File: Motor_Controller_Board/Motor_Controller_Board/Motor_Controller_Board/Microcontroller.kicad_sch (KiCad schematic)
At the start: 26 parts, among them J301 Conn_01x04, J302 USB_B_Micro, J303 Conn_01x02, J304 Conn_01x02, J305 Conn_01x02, SW301 SW_Push, SW302 SW_Push, U301 AMS1117, U302 ESP32-C6-MINI-1

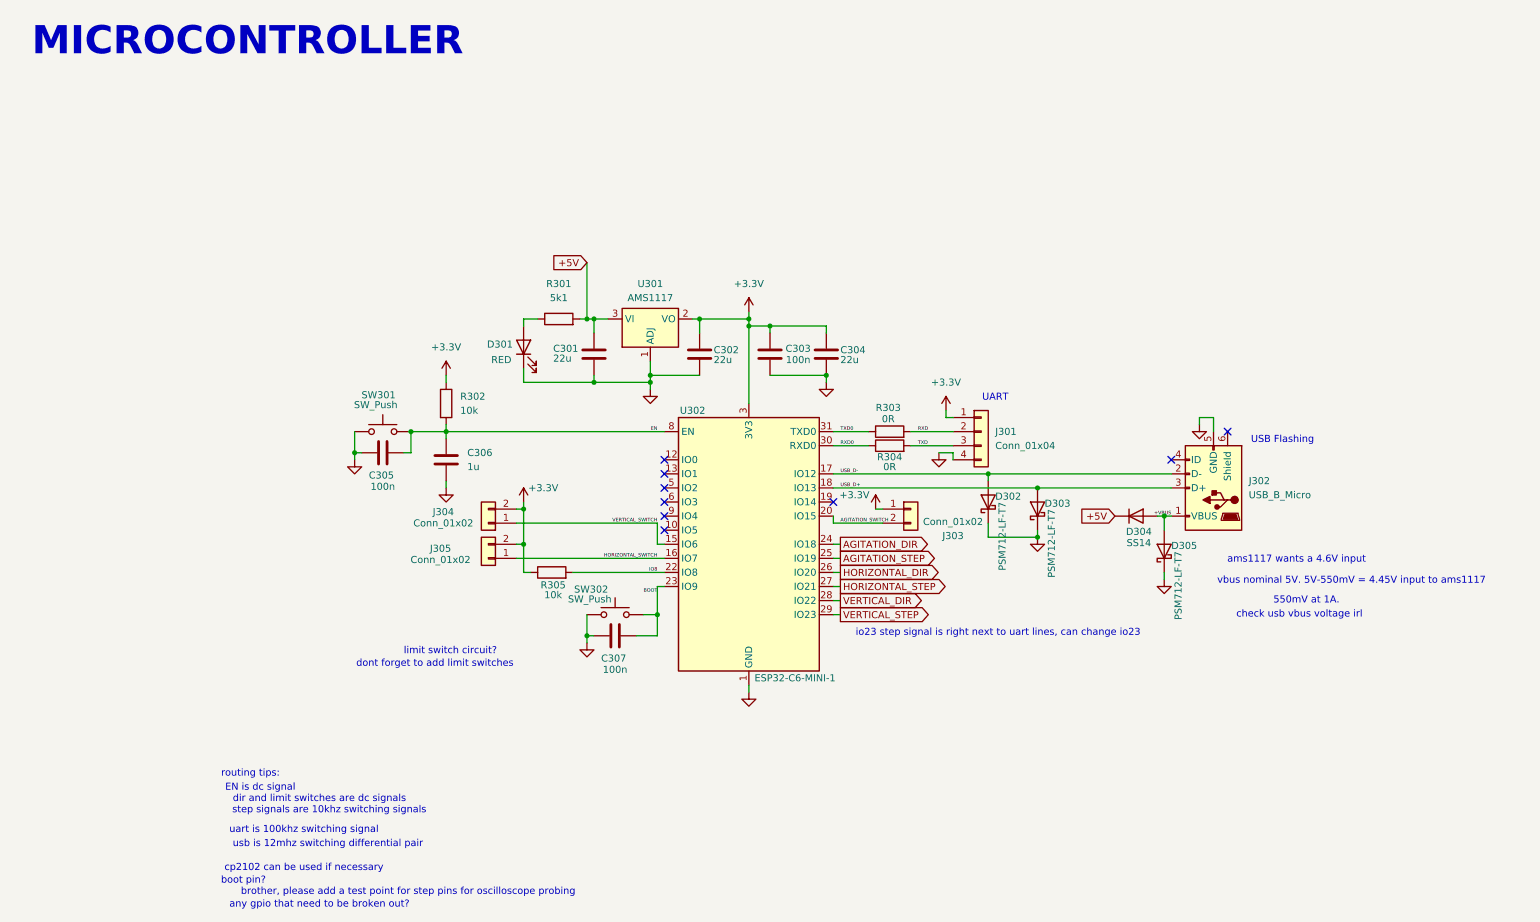
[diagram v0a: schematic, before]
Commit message: discussed with Alex and Mishari. confident in schematic, going to do layout tomorrow
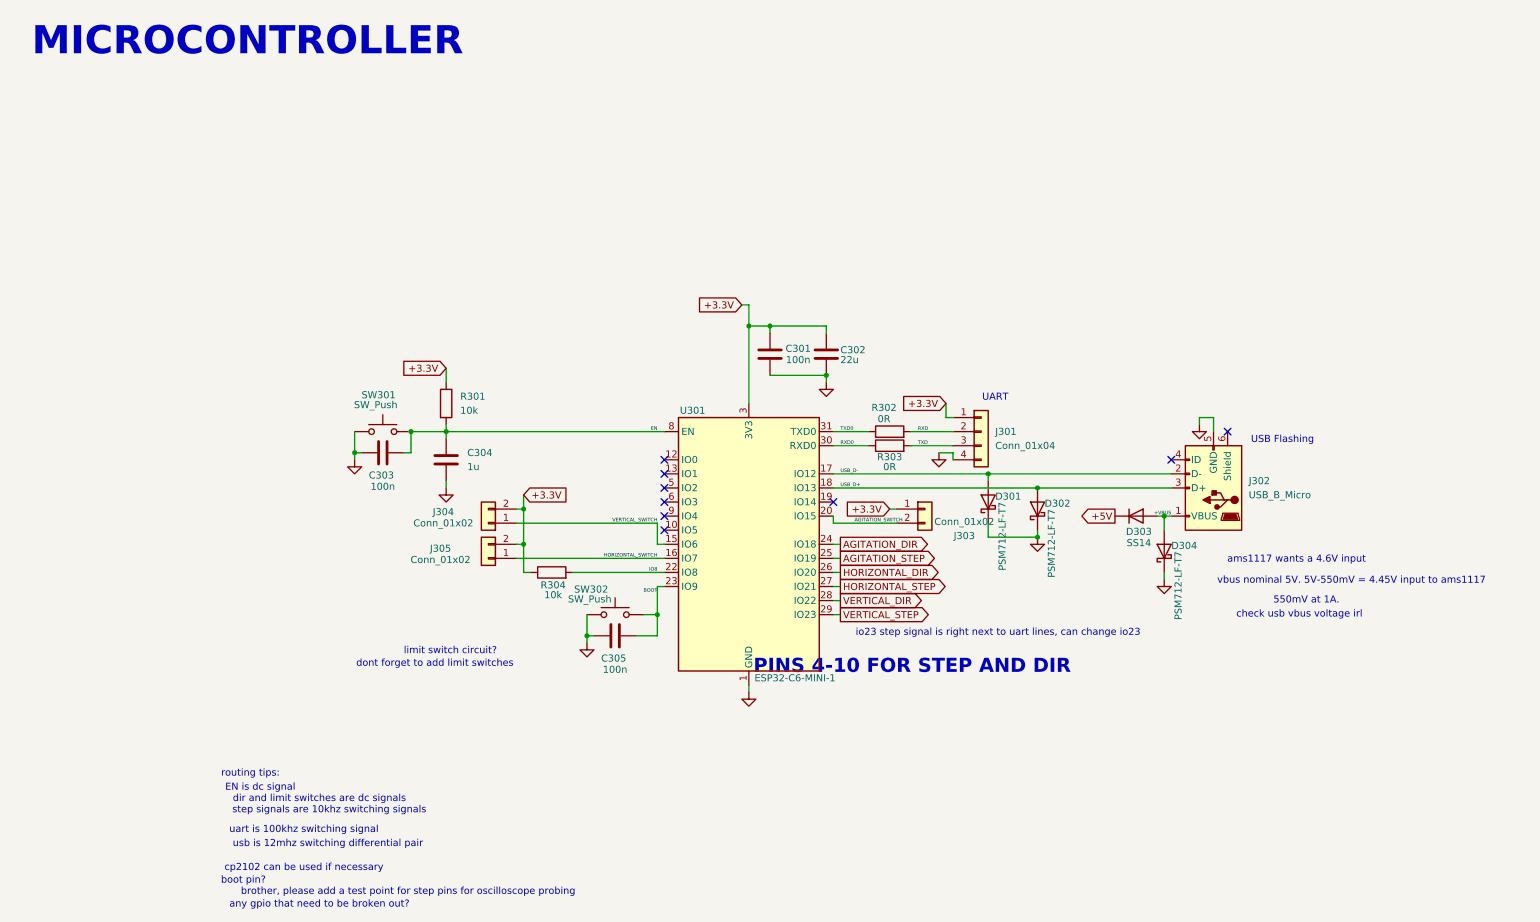
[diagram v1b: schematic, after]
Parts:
- removed C301, C302: 22u, Capacitor_SMD:C_0603_1608Metric, symbol Device:C
- removed D301: RED, LED_SMD:LED_0603_1608Metric, symbol Device:LED
- removed R301: 5k1, Resistor_SMD:R_0603_1608Metric, symbol Device:R
- removed U301: AMS1117, Package_TO_SOT_SMD:SOT-223-3_TabPin2, symbol Regulator_Linear:AMS1117
- renumbered C303 to C301, C304 to C302, C305 to C303, C306 to C304, C307 to C305, D302 to D301, D303 to D302, D304 to D303, D305 to D304, R302 to R301, R303 to R302, R304 to R303, R305 to R304, U302 to U301
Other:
- note added: "PINS 4-10 FOR STEP AND DIR"
- moved on the sheet: J303

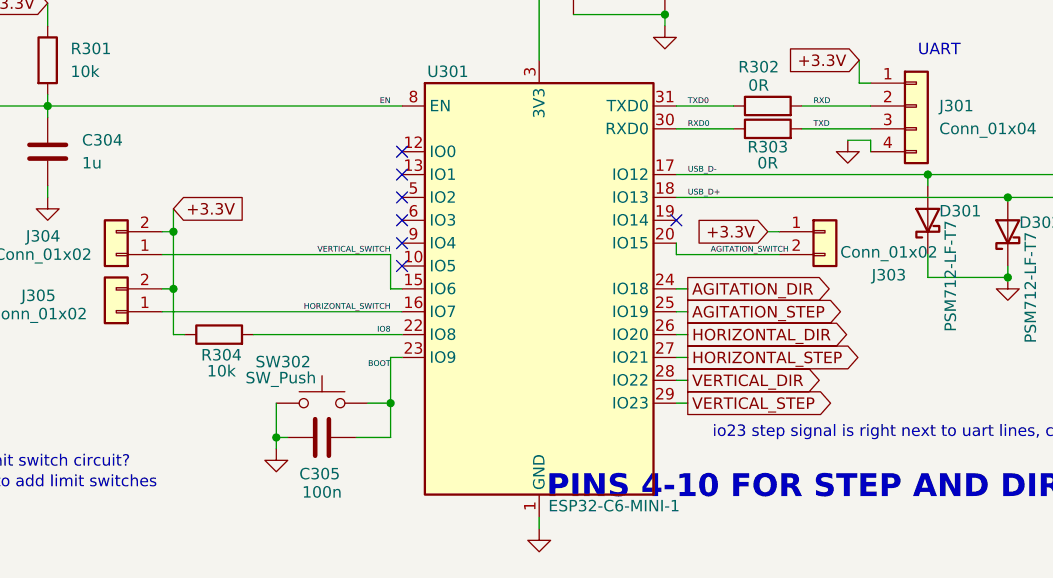
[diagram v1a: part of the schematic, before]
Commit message: routing 75% finished, but very sloppy
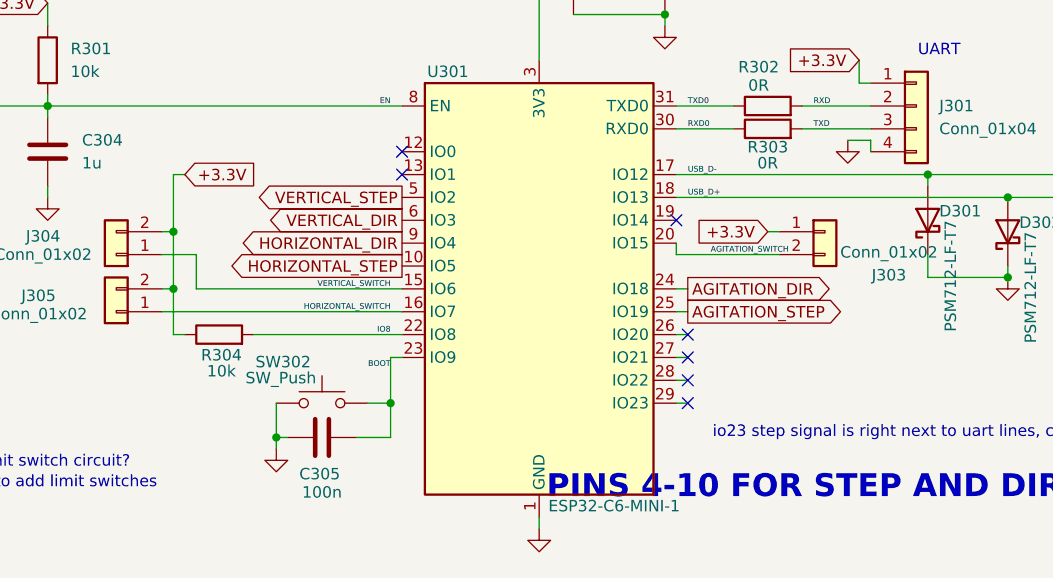
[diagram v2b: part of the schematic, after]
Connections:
- net HORIZONTAL_DIR: now also U301.9 (IO4); no longer U301.26 (IO20)
- net HORIZONTAL_STEP: now also U301.10 (IO5); no longer U301.27 (IO21)
- net VERTICAL_DIR: now also U301.6 (IO3); no longer U301.28 (IO22)
- net VERTICAL_STEP: now also U301.5 (IO2); no longer U301.29 (IO23)
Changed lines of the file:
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@@
+	)
+	(junction
+		(at 101.6 102.87)
+		(diameter 0)
+		(color 0 0 0 0)
 	)
 	(junction
@@
 	)
 	(junction
-		(at 101.6 102.87)
-		(diameter 0)
-		(color 0 0 0 0)
-	)
-	(junction
 		(at 81.28 88.9)
 		(diameter 0)
@@
 	)
 	(no_connect
-		(at 127 104.14)
+		(at 158.75 116.84)
+	)
+	(no_connect
+		(at 158.75 119.38)
 	)
 	(no_connect
@@
 	)
 	(no_connect
-		(at 127 99.06)
+		(at 157.48 101.6)
 	)
 	(no_connect
-		(at 157.48 101.6)
+		(at 158.75 114.3)
 	)
 	(no_connect
-		(at 127 101.6)
+		(at 158.75 121.92)
 	)
 	(no_connect
@@
 		(at 127 96.52)
 	)
-	(no_connect
-		(at 127 106.68)
-	)
 	(wire
 		(pts
@@
 	(wire
 		(pts
+			(xy 101.6 96.52) (xy 101.6 102.87)
+		)
+		(stroke
+			(width 0)
+			(type default)
+		)
+	)
+	(wire
+		(pts
 			(xy 125.73 121.92) (xy 125.73 125.73)
 		)
@@
 	(wire
 		(pts
+			(xy 104.14 109.22) (xy 104.14 105.41)
+		)
+		(stroke
+			(width 0)
+			(type default)
+		)
+	)
+	(wire
+		(pts
 			(xy 142.24 66.04) (xy 142.24 69.85)
 		)
@@
 	(wire
 		(pts
+			(xy 104.14 105.41) (xy 100.33 105.41)
+		)
+		(stroke
+			(width 0)
+			(type default)
+		)
+	)
+	(wire
+		(pts
 			(xy 157.48 116.84) (xy 158.75 116.84)
 		)
@@
 	(wire
 		(pts
+			(xy 104.14 109.22) (xy 127 109.22)
+		)
+		(stroke
+			(width 0)
+			(type default)
+		)
+	)
+	(wire
+		(pts
 			(xy 226.06 86.36) (xy 223.52 86.36)
 		)
@@
 	(wire
 		(pts
-			(xy 101.6 100.33) (xy 101.6 102.87)
-		)
-		(stroke
-			(width 0)
-			(type default)
-		)
-	)
-	(wire
-		(pts
 			(xy 87.63 87.63) (xy 87.63 88.9)
 		)
@@
 	(wire
 		(pts
-			(xy 100.33 105.41) (xy 125.73 105.41)
-		)
-		(stroke
-			(width 0)
-			(type default)
-		)
-	)
-	(wire
-		(pts
 			(xy 87.63 97.79) (xy 87.63 99.06)
 		)
@@
 	(wire
 		(pts
-			(xy 125.73 109.22) (xy 127 109.22)
-		)
-		(stroke
-			(width 0)
-			(type default)
-		)
-	)
-	(wire
-		(pts
 			(xy 157.48 96.52) (xy 185.42 96.52)
 		)
@@
 	(wire
 		(pts
+			(xy 101.6 96.52) (xy 102.87 96.52)
+		)
+		(stroke
+			(width 0)
+			(type default)
+		)
+	)
+	(wire
+		(pts
 			(xy 157.48 91.44) (xy 163.83 91.44)
 		)
@@
 		(pts
 			(xy 113.03 125.73) (xy 113.03 127)
-		)
-		(stroke
-			(width 0)
-			(type default)
-		)
-	)
-	(wire
-		(pts
-			(xy 125.73 105.41) (xy 125.73 109.22)
 		)
 		(stroke
@@
 	)
 	(label "VERTICAL_SWITCH"
-		(at 125.73 105.41 180)
+		(at 125.73 109.22 180)
 		(effects
 			(font
@@
 	(global_label "+3.3V"
 		(shape input)
-		(at 101.6 100.33 0)
+		(at 102.87 96.52 0)
 		(fields_autoplaced yes)
 		(effects
@@
 		)
 		(property "Intersheetrefs" "${INTERSHEET_REFS}"
-			(at 110.27 100.33 0)
+			(at 111.54 96.52 0)
 			(effects
 				(font
@@
 	(global_label "HORIZONTAL_DIR"
 		(shape output)
-		(at 158.75 114.3 0)
+		(at 127 104.14 180)
 		(fields_autoplaced yes)
 		(effects
@@
 				(size 1.27 1.27)
 			)
-			(justify left)
+			(justify right)
 		)
 		(property "Intersheetrefs" "${INTERSHEET_REFS}"
-			(at 177.3382 114.3 0)
+			(at 108.4118 104.14 0)
 			(effects
 				(font
 					(size 1.27 1.27)
 				)
-				(justify left)
+				(justify right)
 				(hide yes)
 			)
@@
 	(global_label "HORIZONTAL_STEP"
 		(shape output)
-		(at 158.75 116.84 0)
+		(at 127 106.68 180)
 		(fields_autoplaced yes)
 		(effects
@@
 				(size 1.27 1.27)
 			)
-			(justify left)
+			(justify right)
 		)
 		(property "Intersheetrefs" "${INTERSHEET_REFS}"
-			(at 178.7895 116.84 0)
+			(at 106.9605 106.68 0)
 			(effects
 				(font
 					(size 1.27 1.27)
 				)
-				(justify left)
+				(justify right)
 				(hide yes)
 			)
@@
 	(global_label "VERTICAL_DIR"
 		(shape output)
-		(at 158.75 119.38 0)
+		(at 127 101.6 180)
 		(fields_autoplaced yes)
 		(effects
@@
 				(size 1.27 1.27)
 			)
-			(justify left)
+			(justify right)
 		)
 		(property "Intersheetrefs" "${INTERSHEET_REFS}"
-			(at 174.3143 119.38 0)
+			(at 111.4357 101.6 0)
 			(effects
 				(font
 					(size 1.27 1.27)
 				)
-				(justify left)
+				(justify right)
 				(hide yes)
 			)
@@
 	(global_label "VERTICAL_STEP"
 		(shape output)
-		(at 158.75 121.92 0)
+		(at 127 99.06 180)
 		(fields_autoplaced yes)
 		(effects
@@
 				(size 1.27 1.27)
 			)
-			(justify left)
+			(justify right)
 		)
 		(property "Intersheetrefs" "${INTERSHEET_REFS}"
-			(at 175.7656 121.92 0)
+			(at 109.9844 99.06 0)
 			(effects
 				(font
 					(size 1.27 1.27)
 				)
-				(justify left)
+				(justify right)
 				(hide yes)
 			)
